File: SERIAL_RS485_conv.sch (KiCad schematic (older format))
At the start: 12 parts

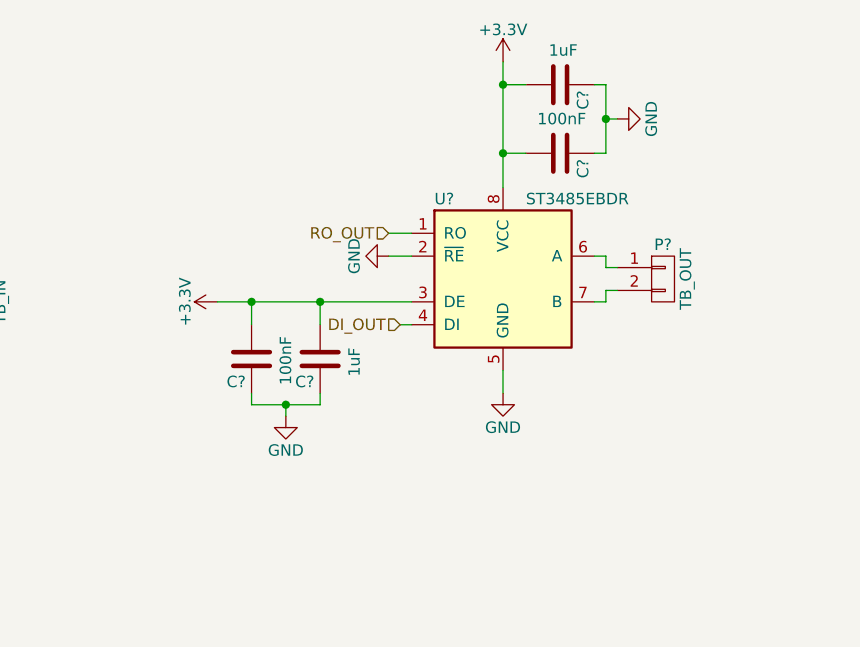
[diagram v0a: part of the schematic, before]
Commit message: Added to scheamtic.
Added reset circuit for Aiya, power led for 3V3 line, USB type A connectors for USBB and USBC.
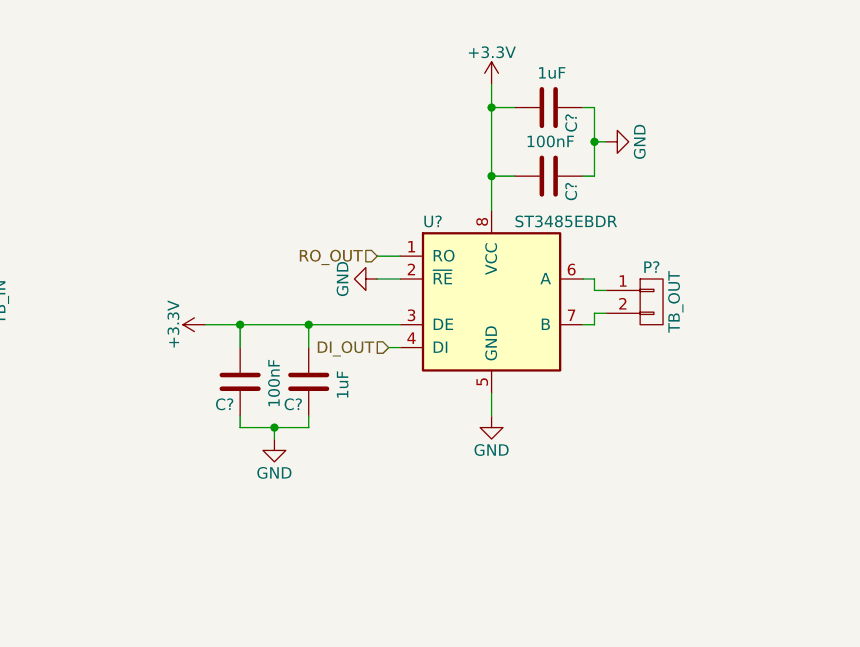
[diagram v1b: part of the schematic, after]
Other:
- moved on the sheet: C?, P?, U?
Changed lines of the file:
@@
 LIBS:w_connectors
 LIBS:max-lin
+LIBS:IHE
 LIBS:E-GIF-M-Board-cache
 EELAYER 25 0
@@
 L ST3485EBDR U?
 U 1 1 588FE75F
-P 7100 3950
-F 0 "U?" H 6800 4300 50  0000 L CNN
-F 1 "ST3485EBDR" H 7200 4300 50  0000 L CNN
-F 2 "Housings_SO8" H 7450 3600 50  0001 C CIN
-F 3 "" H 7100 3950 50  0000 C CNN
-	1    7100 3950
+P 7050 4050
+F 0 "U?" H 6750 4400 50  0000 L CNN
+F 1 "ST3485EBDR" H 7150 4400 50  0000 L CNN
+F 2 "Housings_SO8" H 7400 3700 50  0001 C CIN
+F 3 "" H 7050 4050 50  0000 C CNN
+	1    7050 4050
 	1    0    0    -1
 $EndComp
@@
 L +3.3V #PWR061
 U 1 1 588FEB3E
-P 7100 3000
-F 0 "#PWR061" H 7100 2850 50  0001 C CNN
-F 1 "+3.3V" H 7100 3140 50  0000 C CNN
-F 2 "" H 7100 3000 50  0000 C CNN
-F 3 "" H 7100 3000 50  0000 C CNN
-	1    7100 3000
+P 7050 3100
+F 0 "#PWR061" H 7050 2950 50  0001 C CNN
+F 1 "+3.3V" H 7050 3240 50  0000 C CNN
+F 2 "" H 7050 3100 50  0000 C CNN
+F 3 "" H 7050 3100 50  0000 C CNN
+	1    7050 3100
 	1    0    0    -1
 $EndComp
@@
 L C C?
 U 1 1 588FEB44
-P 7350 3100
-F 0 "C?" H 7375 3200 50  0000 L CNN
-F 1 "1uF" V 7200 3050 50  0000 L CNN
-F 2 "" H 7388 2950 50  0000 C CNN
-F 3 "" H 7350 3100 50  0000 C CNN
-	1    7350 3100
+P 7300 3200
+F 0 "C?" H 7325 3300 50  0000 L CNN
+F 1 "1uF" V 7150 3150 50  0000 L CNN
+F 2 "" H 7338 3050 50  0000 C CNN
+F 3 "" H 7300 3200 50  0000 C CNN
+	1    7300 3200
 	0    1    1    0
 $EndComp
@@
 L C C?
 U 1 1 588FEB4A
-P 7350 3400
-F 0 "C?" H 7375 3500 50  0000 L CNN
-F 1 "100nF" V 7200 3300 50  0000 L CNN
-F 2 "" H 7388 3250 50  0000 C CNN
-F 3 "" H 7350 3400 50  0000 C CNN
-	1    7350 3400
+P 7300 3500
+F 0 "C?" H 7325 3600 50  0000 L CNN
+F 1 "100nF" V 7150 3400 50  0000 L CNN
+F 2 "" H 7338 3350 50  0000 C CNN
+F 3 "" H 7300 3500 50  0000 C CNN
+	1    7300 3500
 	0    1    1    0
 $EndComp
@@
 L GND #PWR062
 U 1 1 588FEB50
-P 7600 3250
-F 0 "#PWR062" H 7600 3000 50  0001 C CNN
-F 1 "GND" H 7600 3100 50  0000 C CNN
-F 2 "" H 7600 3250 50  0000 C CNN
-F 3 "" H 7600 3250 50  0000 C CNN
-	1    7600 3250
+P 7550 3350
+F 0 "#PWR062" H 7550 3100 50  0001 C CNN
+F 1 "GND" H 7550 3200 50  0000 C CNN
+F 2 "" H 7550 3350 50  0000 C CNN
+F 3 "" H 7550 3350 50  0000 C CNN
+	1    7550 3350
 	0    -1   -1   0
 $EndComp
 Wire Wire Line
-	7100 3000 7100 3550
-Wire Wire Line
-	7100 3100 7200 3100
-Wire Wire Line
-	7100 3400 7200 3400
-Connection ~ 7100 3100
-Connection ~ 7100 3400
-Wire Wire Line
-	7600 3250 7550 3250
-Wire Wire Line
-	7550 3100 7550 3400
-Wire Wire Line
-	7550 3100 7500 3100
-Wire Wire Line
-	7550 3400 7500 3400
-Connection ~ 7550 3250
+	7050 3100 7050 3650
+Wire Wire Line
+	7050 3200 7150 3200
+Wire Wire Line
+	7050 3500 7150 3500
+Connection ~ 7050 3200
+Connection ~ 7050 3500
+Wire Wire Line
+	7550 3350 7500 3350
+Wire Wire Line
+	7500 3200 7500 3500
+Wire Wire Line
+	7500 3200 7450 3200
+Wire Wire Line
+	7500 3500 7450 3500
+Connection ~ 7500 3350
 $Comp
 L CONN_01X02 P?
 U 1 1 588FEC2E
-P 7800 3950
-F 0 "P?" H 7800 4100 50  0000 C CNN
-F 1 "TB_OUT" V 7900 3950 50  0000 C CNN
-F 2 "" H 7800 3950 50  0000 C CNN
-F 3 "" H 7800 3950 50  0000 C CNN
-	1    7800 3950
+P 7750 4050
+F 0 "P?" H 7750 4200 50  0000 C CNN
+F 1 "TB_OUT" V 7850 4050 50  0000 C CNN
+F 2 "" H 7750 4050 50  0000 C CNN
+F 3 "" H 7750 4050 50  0000 C CNN
+	1    7750 4050
 	1    0    0    -1
 $EndComp
@@
 $EndComp
 Wire Wire Line
-	7500 3850 7550 3850
-Wire Wire Line
-	7550 3850 7550 3900
-Wire Wire Line
-	7550 3900 7600 3900
-Wire Wire Line
-	7500 4050 7550 4050
-Wire Wire Line
-	7550 4050 7550 4000
-Wire Wire Line
-	7550 4000 7600 4000
+	7450 3950 7500 3950
+Wire Wire Line
+	7500 3950 7500 4000
+Wire Wire Line
+	7500 4000 7550 4000
+Wire Wire Line
+	7450 4150 7500 4150
+Wire Wire Line
+	7500 4150 7500 4100
+Wire Wire Line
+	7500 4100 7550 4100
 Wire Wire Line
 	4500 3950 4550 3950
@@
 L GND #PWR064
 U 1 1 588FEEFA
-P 7100 4450
-F 0 "#PWR064" H 7100 4200 50  0001 C CNN
-F 1 "GND" H 7100 4300 50  0000 C CNN
-F 2 "" H 7100 4450 50  0000 C CNN
-F 3 "" H 7100 4450 50  0000 C CNN
-	1    7100 4450
-	1    0    0    -1
-$EndComp
-Wire Wire Line
-	7100 4450 7100 4350
+P 7050 4550
+F 0 "#PWR064" H 7050 4300 50  0001 C CNN
+F 1 "GND" H 7050 4400 50  0000 C CNN
+F 2 "" H 7050 4550 50  0000 C CNN
+F 3 "" H 7050 4550 50  0000 C CNN
+	1    7050 4550
+	1    0    0    -1
+$EndComp
+Wire Wire Line
+	7050 4550 7050 4450
 Wire Wire Line
 	4100 4550 4100 4450
@@
 L GND #PWR068
 U 1 1 588FFC3B
-P 6600 3850
-F 0 "#PWR068" H 6600 3600 50  0001 C CNN
-F 1 "GND" H 6600 3700 50  0000 C CNN
-F 2 "" H 6600 3850 50  0000 C CNN
-F 3 "" H 6600 3850 50  0000 C CNN
-	1    6600 3850
-	0    1    1    0
-$EndComp
-Wire Wire Line
-	6600 3850 6700 3850
-Text HLabel 6600 3750 0    50   Input ~ 0
+P 6550 3950
+F 0 "#PWR068" H 6550 3700 50  0001 C CNN
+F 1 "GND" H 6550 3800 50  0000 C CNN
+F 2 "" H 6550 3950 50  0000 C CNN
+F 3 "" H 6550 3950 50  0000 C CNN
+	1    6550 3950
+	0    1    1    0
+$EndComp
+Wire Wire Line
+	6550 3950 6650 3950
+Text HLabel 6550 3850 0    50   Input ~ 0
 RO_OUT
-Text HLabel 6650 4150 0    50   Input ~ 0
+Text HLabel 6600 4250 0    50   Input ~ 0
 DI_OUT
 $Comp
 L +3.3V #PWR069
 U 1 1 588FFF45
-P 5850 4050
-F 0 "#PWR069" H 5850 3900 50  0001 C CNN
-F 1 "+3.3V" H 5850 4190 50  0000 C CNN
-F 2 "" H 5850 4050 50  0000 C CNN
-F 3 "" H 5850 4050 50  0000 C CNN
-	1    5850 4050
+P 5800 4150
+F 0 "#PWR069" H 5800 4000 50  0001 C CNN
+F 1 "+3.3V" H 5800 4290 50  0000 C CNN
+F 2 "" H 5800 4150 50  0000 C CNN
+F 3 "" H 5800 4150 50  0000 C CNN
+	1    5800 4150
 	0    -1   -1   0
 $EndComp
@@
 L C C?
 U 1 1 588FFF4B
-P 6300 4300
-F 0 "C?" H 6325 4400 50  0000 L CNN
-F 1 "1uF" V 6150 4250 50  0000 L CNN
-F 2 "" H 6338 4150 50  0000 C CNN
-F 3 "" H 6300 4300 50  0000 C CNN
-	1    6300 4300
+P 6250 4400
+F 0 "C?" H 6275 4500 50  0000 L CNN
+F 1 "1uF" V 6100 4350 50  0000 L CNN
+F 2 "" H 6288 4250 50  0000 C CNN
+F 3 "" H 6250 4400 50  0000 C CNN
+	1    6250 4400
 	-1   0    0    1
 $EndComp
@@
 L C C?
 U 1 1 588FFF51
-P 6000 4300
-F 0 "C?" H 6025 4400 50  0000 L CNN
-F 1 "100nF" V 5850 4200 50  0000 L CNN
-F 2 "" H 6038 4150 50  0000 C CNN
-F 3 "" H 6000 4300 50  0000 C CNN
-	1    6000 4300
+P 5950 4400
+F 0 "C?" H 5975 4500 50  0000 L CNN
+F 1 "100nF" V 5800 4300 50  0000 L CNN
+F 2 "" H 5988 4250 50  0000 C CNN
+F 3 "" H 5950 4400 50  0000 C CNN
+	1    5950 4400
 	-1   0    0    1
 $EndComp
@@
 L GND #PWR070
 U 1 1 588FFF57
-P 6150 4550
-F 0 "#PWR070" H 6150 4300 50  0001 C CNN
-F 1 "GND" H 6150 4400 50  0000 C CNN
-F 2 "" H 6150 4550 50  0000 C CNN
-F 3 "" H 6150 4550 50  0000 C CNN
-	1    6150 4550
-	1    0    0    -1
-$EndComp
-Wire Wire Line
-	6300 4050 6300 4150
-Wire Wire Line
-	6000 4050 6000 4150
-Connection ~ 6300 4050
-Connection ~ 6000 4050
-Wire Wire Line
-	6150 4550 6150 4500
-Wire Wire Line
-	6300 4500 6000 4500
-Wire Wire Line
-	6300 4500 6300 4450
-Wire Wire Line
-	6000 4500 6000 4450
-Connection ~ 6150 4500
-Wire Wire Line
-	5850 4050 6700 4050
-Wire Wire Line
-	6650 4150 6700 4150
+P 6100 4650
+F 0 "#PWR070" H 6100 4400 50  0001 C CNN
+F 1 "GND" H 6100 4500 50  0000 C CNN
+F 2 "" H 6100 4650 50  0000 C CNN
+F 3 "" H 6100 4650 50  0000 C CNN
+	1    6100 4650
+	1    0    0    -1
+$EndComp
+Wire Wire Line
+	6250 4150 6250 4250
+Wire Wire Line
+	5950 4150 5950 4250
+Connection ~ 6250 4150
+Connection ~ 5950 4150
+Wire Wire Line
+	6100 4650 6100 4600
+Wire Wire Line
+	6250 4600 5950 4600
+Wire Wire Line
+	6250 4600 6250 4550
+Wire Wire Line
+	5950 4600 5950 4550
+Connection ~ 6100 4600
+Wire Wire Line
+	5800 4150 6650 4150
+Wire Wire Line
+	6600 4250 6650 4250
 Text Notes 7000 6750 0    50   ~ 0
 RO is enabled when RE is low.
@@
 The driver outputs are enabled by bringing DE high.
 Wire Wire Line
-	6600 3750 6700 3750
+	6550 3850 6650 3850
 $EndSCHEMATC

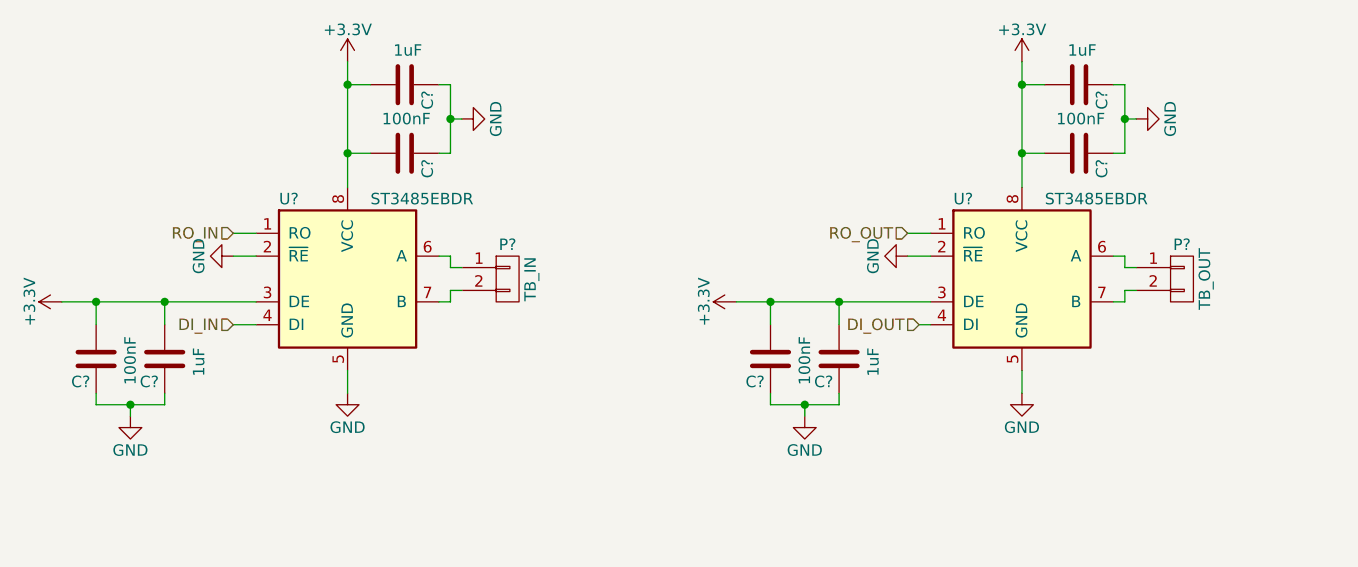
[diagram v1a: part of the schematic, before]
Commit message: Schematic correction
Corrected the direction on some signals. Added a pin header for general development.
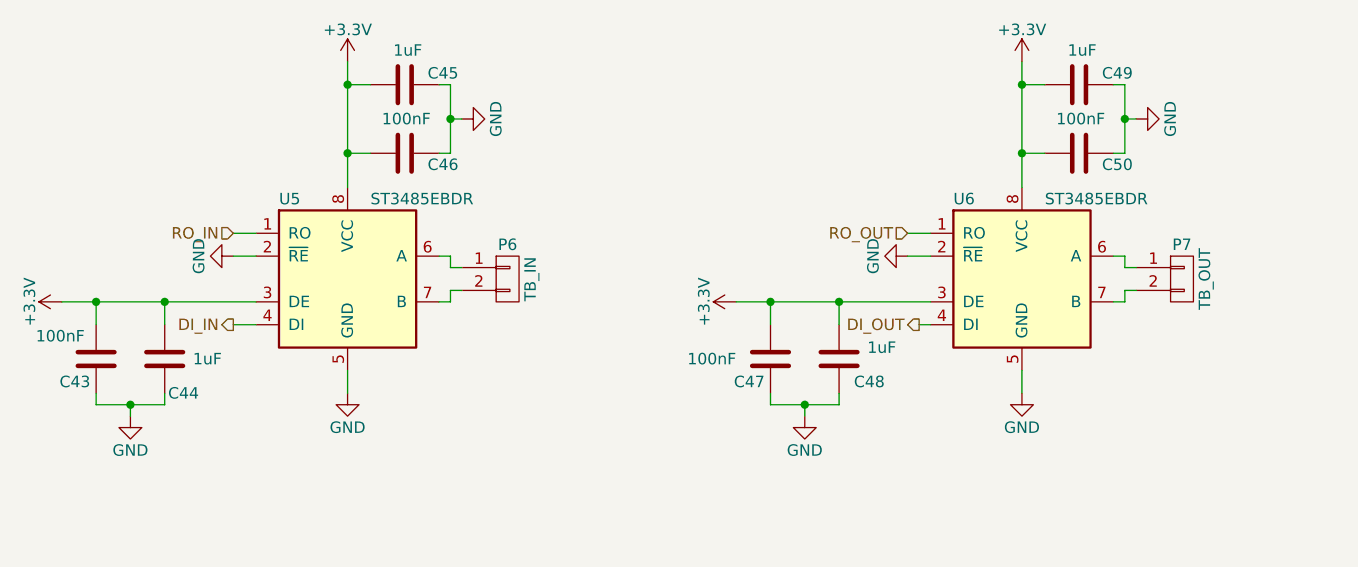
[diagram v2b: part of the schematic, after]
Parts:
- C43, C44, C45, C46, C47, C48, C49, C50: renamed from C?; footprint (none) -> Capacitors_SMD:C_0603_HandSoldering
- gave numbers to parts that had none: 4
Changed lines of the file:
@@
 $Descr A4 11693 8268
 encoding utf-8
-Sheet 7 7
+Sheet 6 7
 Title ""
 Date ""
@@
 $EndDescr
 $Comp
-L ST3485EBDR U?
+L ST3485EBDR U5
 U 1 1 588FE71F
 P 4100 4050
-F 0 "U?" H 3800 4400 50  0000 L CNN
+F 0 "U5" H 3800 4400 50  0000 L CNN
 F 1 "ST3485EBDR" H 4200 4400 50  0000 L CNN
 F 2 "Housings_SO8" H 4450 3700 50  0001 C CIN
@@
 $EndComp
 $Comp
-L ST3485EBDR U?
+L ST3485EBDR U6
 U 1 1 588FE75F
 P 7050 4050
-F 0 "U?" H 6750 4400 50  0000 L CNN
+F 0 "U6" H 6750 4400 50  0000 L CNN
 F 1 "ST3485EBDR" H 7150 4400 50  0000 L CNN
 F 2 "Housings_SO8" H 7400 3700 50  0001 C CIN
@@
 $EndComp
 $Comp
-L +3.3V #PWR059
+L +3.3V #PWR074
 U 1 1 588FE7B3
 P 4100 3100
-F 0 "#PWR059" H 4100 2950 50  0001 C CNN
+F 0 "#PWR074" H 4100 2950 50  0001 C CNN
 F 1 "+3.3V" H 4100 3240 50  0000 C CNN
 F 2 "" H 4100 3100 50  0000 C CNN
@@
 $EndComp
 $Comp
-L C C?
+L C C45
 U 1 1 588FE822
 P 4350 3200
-F 0 "C?" H 4375 3300 50  0000 L CNN
+F 0 "C45" V 4300 3300 50  0000 L CNN
 F 1 "1uF" V 4200 3150 50  0000 L CNN
-F 2 "" H 4388 3050 50  0000 C CNN
+F 2 "Capacitors_SMD:C_0603_HandSoldering" H 4388 3050 50  0001 C CNN
 F 3 "" H 4350 3200 50  0000 C CNN
 	1    4350 3200
@@
 $EndComp
 $Comp
-L C C?
+L C C46
 U 1 1 588FE88A
 P 4350 3500
-F 0 "C?" H 4375 3600 50  0000 L CNN
+F 0 "C46" V 4400 3600 50  0000 L CNN
 F 1 "100nF" V 4200 3400 50  0000 L CNN
-F 2 "" H 4388 3350 50  0000 C CNN
+F 2 "Capacitors_SMD:C_0603_HandSoldering" H 4388 3350 50  0001 C CNN
 F 3 "" H 4350 3500 50  0000 C CNN
 	1    4350 3500
@@
 $EndComp
 $Comp
-L GND #PWR060
+L GND #PWR075
 U 1 1 588FEA04
 P 4600 3350
-F 0 "#PWR060" H 4600 3100 50  0001 C CNN
+F 0 "#PWR075" H 4600 3100 50  0001 C CNN
 F 1 "GND" H 4600 3200 50  0000 C CNN
 F 2 "" H 4600 3350 50  0000 C CNN
@@
 Connection ~ 4550 3350
 $Comp
-L +3.3V #PWR061
+L +3.3V #PWR076
 U 1 1 588FEB3E
 P 7050 3100
-F 0 "#PWR061" H 7050 2950 50  0001 C CNN
+F 0 "#PWR076" H 7050 2950 50  0001 C CNN
 F 1 "+3.3V" H 7050 3240 50  0000 C CNN
 F 2 "" H 7050 3100 50  0000 C CNN
@@
 $EndComp
 $Comp
-L C C?
+L C C49
 U 1 1 588FEB44
 P 7300 3200
-F 0 "C?" H 7325 3300 50  0000 L CNN
+F 0 "C49" V 7250 3300 50  0000 L CNN
 F 1 "1uF" V 7150 3150 50  0000 L CNN
-F 2 "" H 7338 3050 50  0000 C CNN
+F 2 "Capacitors_SMD:C_0603_HandSoldering" H 7338 3050 50  0001 C CNN
 F 3 "" H 7300 3200 50  0000 C CNN
 	1    7300 3200
@@
 $EndComp
 $Comp
-L C C?
+L C C50
 U 1 1 588FEB4A
 P 7300 3500
-F 0 "C?" H 7325 3600 50  0000 L CNN
+F 0 "C50" V 7350 3600 50  0000 L CNN
 F 1 "100nF" V 7150 3400 50  0000 L CNN
-F 2 "" H 7338 3350 50  0000 C CNN
+F 2 "Capacitors_SMD:C_0603_HandSoldering" H 7338 3350 50  0001 C CNN
 F 3 "" H 7300 3500 50  0000 C CNN
 	1    7300 3500
@@
 $EndComp
 $Comp
-L GND #PWR062
+L GND #PWR077
 U 1 1 588FEB50
 P 7550 3350
-F 0 "#PWR062" H 7550 3100 50  0001 C CNN
+F 0 "#PWR077" H 7550 3100 50  0001 C CNN
 F 1 "GND" H 7550 3200 50  0000 C CNN
 F 2 "" H 7550 3350 50  0000 C CNN
@@
 Connection ~ 7500 3350
 $Comp
-L CONN_01X02 P?
+L CONN_01X02 P7
 U 1 1 588FEC2E
 P 7750 4050
-F 0 "P?" H 7750 4200 50  0000 C CNN
+F 0 "P7" H 7750 4200 50  0000 C CNN
 F 1 "TB_OUT" V 7850 4050 50  0000 C CNN
-F 2 "" H 7750 4050 50  0000 C CNN
+F 2 "" H 7750 4050 50  0001 C CNN
 F 3 "" H 7750 4050 50  0000 C CNN
 	1    7750 4050
@@
 $EndComp
 $Comp
-L CONN_01X02 P?
+L CONN_01X02 P6
 U 1 1 588FECFB
 P 4800 4050
-F 0 "P?" H 4800 4200 50  0000 C CNN
+F 0 "P6" H 4800 4200 50  0000 C CNN
 F 1 "TB_IN" V 4900 4050 50  0000 C CNN
-F 2 "" H 4800 4050 50  0000 C CNN
+F 2 "" H 4800 4050 50  0001 C CNN
 F 3 "" H 4800 4050 50  0000 C CNN
 	1    4800 4050
@@
 	4550 4100 4600 4100
 $Comp
-L GND #PWR063
+L GND #PWR078
 U 1 1 588FEED7
 P 4100 4550
-F 0 "#PWR063" H 4100 4300 50  0001 C CNN
+F 0 "#PWR078" H 4100 4300 50  0001 C CNN
 F 1 "GND" H 4100 4400 50  0000 C CNN
 F 2 "" H 4100 4550 50  0000 C CNN
@@
 $EndComp
 $Comp
-L GND #PWR064
+L GND #PWR079
 U 1 1 588FEEFA
 P 7050 4550
-F 0 "#PWR064" H 7050 4300 50  0001 C CNN
+F 0 "#PWR079" H 7050 4300 50  0001 C CNN
 F 1 "GND" H 7050 4400 50  0000 C CNN
 F 2 "" H 7050 4550 50  0000 C CNN
@@
 	4100 4550 4100 4450
 $Comp
-L +3.3V #PWR065
+L +3.3V #PWR080
 U 1 1 588FF500
 P 2850 4150
-F 0 "#PWR065" H 2850 4000 50  0001 C CNN
+F 0 "#PWR080" H 2850 4000 50  0001 C CNN
 F 1 "+3.3V" H 2850 4290 50  0000 C CNN
 F 2 "" H 2850 4150 50  0000 C CNN
@@
 $EndComp
 $Comp
-L C C?
+L C C44
 U 1 1 588FF506
 P 3300 4400
-F 0 "C?" H 3325 4500 50  0000 L CNN
-F 1 "1uF" V 3150 4350 50  0000 L CNN
-F 2 "" H 3338 4250 50  0000 C CNN
+F 0 "C44" H 3150 4550 50  0000 L CNN
+F 1 "1uF" H 3050 4400 50  0000 L CNN
+F 2 "Capacitors_SMD:C_0603_HandSoldering" H 3338 4250 50  0001 C CNN
 F 3 "" H 3300 4400 50  0000 C CNN
 	1    3300 4400
@@
 $EndComp
 $Comp
-L C C?
+L C C43
 U 1 1 588FF50C
 P 3000 4400
-F 0 "C?" H 3025 4500 50  0000 L CNN
-F 1 "100nF" V 2850 4300 50  0000 L CNN
-F 2 "" H 3038 4250 50  0000 C CNN
+F 0 "C43" H 3025 4500 50  0000 L CNN
+F 1 "100nF" H 3050 4300 50  0000 L CNN
+F 2 "Capacitors_SMD:C_0603_HandSoldering" H 3038 4250 50  0001 C CNN
 F 3 "" H 3000 4400 50  0000 C CNN
 	1    3000 4400
@@
 $EndComp
 $Comp
-L GND #PWR066
+L GND #PWR081
 U 1 1 588FF512
 P 3150 4650
-F 0 "#PWR066" H 3150 4400 50  0001 C CNN
+F 0 "#PWR081" H 3150 4400 50  0001 C CNN
 F 1 "GND" H 3150 4500 50  0000 C CNN
 F 2 "" H 3150 4650 50  0000 C CNN
@@
 Wire Wire Line
 	2850 4150 3700 4150
-Text HLabel 3600 4250 0    50   Input ~ 0
+Text HLabel 3600 4250 0    50   Output ~ 0
 DI_IN
 Text HLabel 3600 3850 0    50   Input ~ 0
@@
 	3600 4250 3700 4250
 $Comp
-L GND #PWR067
+L GND #PWR082
 U 1 1 588FFA34
 P 3600 3950
-F 0 "#PWR067" H 3600 3700 50  0001 C CNN
+F 0 "#PWR082" H 3600 3700 50  0001 C CNN
 F 1 "GND" H 3600 3800 50  0000 C CNN
 F 2 "" H 3600 3950 50  0000 C CNN
@@
 	3600 3950 3700 3950
 $Comp
-L GND #PWR068
+L GND #PWR083
 U 1 1 588FFC3B
 P 6550 3950
-F 0 "#PWR068" H 6550 3700 50  0001 C CNN
+F 0 "#PWR083" H 6550 3700 50  0001 C CNN
 F 1 "GND" H 6550 3800 50  0000 C CNN
 F 2 "" H 6550 3950 50  0000 C CNN
@@
 Text HLabel 6550 3850 0    50   Input ~ 0
 RO_OUT
-Text HLabel 6600 4250 0    50   Input ~ 0
+Text HLabel 6600 4250 0    50   Output ~ 0
 DI_OUT
 $Comp
-L +3.3V #PWR069
+L +3.3V #PWR084
 U 1 1 588FFF45
 P 5800 4150
-F 0 "#PWR069" H 5800 4000 50  0001 C CNN
+F 0 "#PWR084" H 5800 4000 50  0001 C CNN
 F 1 "+3.3V" H 5800 4290 50  0000 C CNN
 F 2 "" H 5800 4150 50  0000 C CNN
@@
 $EndComp
 $Comp
-L C C?
+L C C48
 U 1 1 588FFF4B
 P 6250 4400
-F 0 "C?" H 6275 4500 50  0000 L CNN
-F 1 "1uF" V 6100 4350 50  0000 L CNN
-F 2 "" H 6288 4250 50  0000 C CNN
+F 0 "C48" H 6050 4500 50  0000 L CNN
+F 1 "1uF" H 6000 4350 50  0000 L CNN
+F 2 "Capacitors_SMD:C_0603_HandSoldering" H 6288 4250 50  0001 C CNN
 F 3 "" H 6250 4400 50  0000 C CNN
 	1    6250 4400
@@
 $EndComp
 $Comp
-L C C?
+L C C47
 U 1 1 588FFF51
 P 5950 4400
-F 0 "C?" H 5975 4500 50  0000 L CNN
-F 1 "100nF" V 5800 4300 50  0000 L CNN
-F 2 "" H 5988 4250 50  0000 C CNN
+F 0 "C47" H 5975 4500 50  0000 L CNN
+F 1 "100nF" H 6100 4400 50  0000 L CNN
+F 2 "Capacitors_SMD:C_0603_HandSoldering" H 5988 4250 50  0001 C CNN
 F 3 "" H 5950 4400 50  0000 C CNN
 	1    5950 4400
@@
 $EndComp
 $Comp
-L GND #PWR070
+L GND #PWR085
 U 1 1 588FFF57
 P 6100 4650
-F 0 "#PWR070" H 6100 4400 50  0001 C CNN
+F 0 "#PWR085" H 6100 4400 50  0001 C CNN
 F 1 "GND" H 6100 4500 50  0000 C CNN
 F 2 "" H 6100 4650 50  0000 C CNN
